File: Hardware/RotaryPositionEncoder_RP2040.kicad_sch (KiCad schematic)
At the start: 66 parts, among them J1 Conn_ABI, J2 Conn_UVW, J3 Conn_SWD, J4 USB_C_Receptacle_USB2.0, J5 Conn_5VDC, J6 Conn_CAN, U1 AS5047P, U2 RP2040, U3 M24C02-RMN, U3 RT9013-33GB, U4 W25Q32JVSS, U5 TJA1042T, Y1 Crystal_GND24

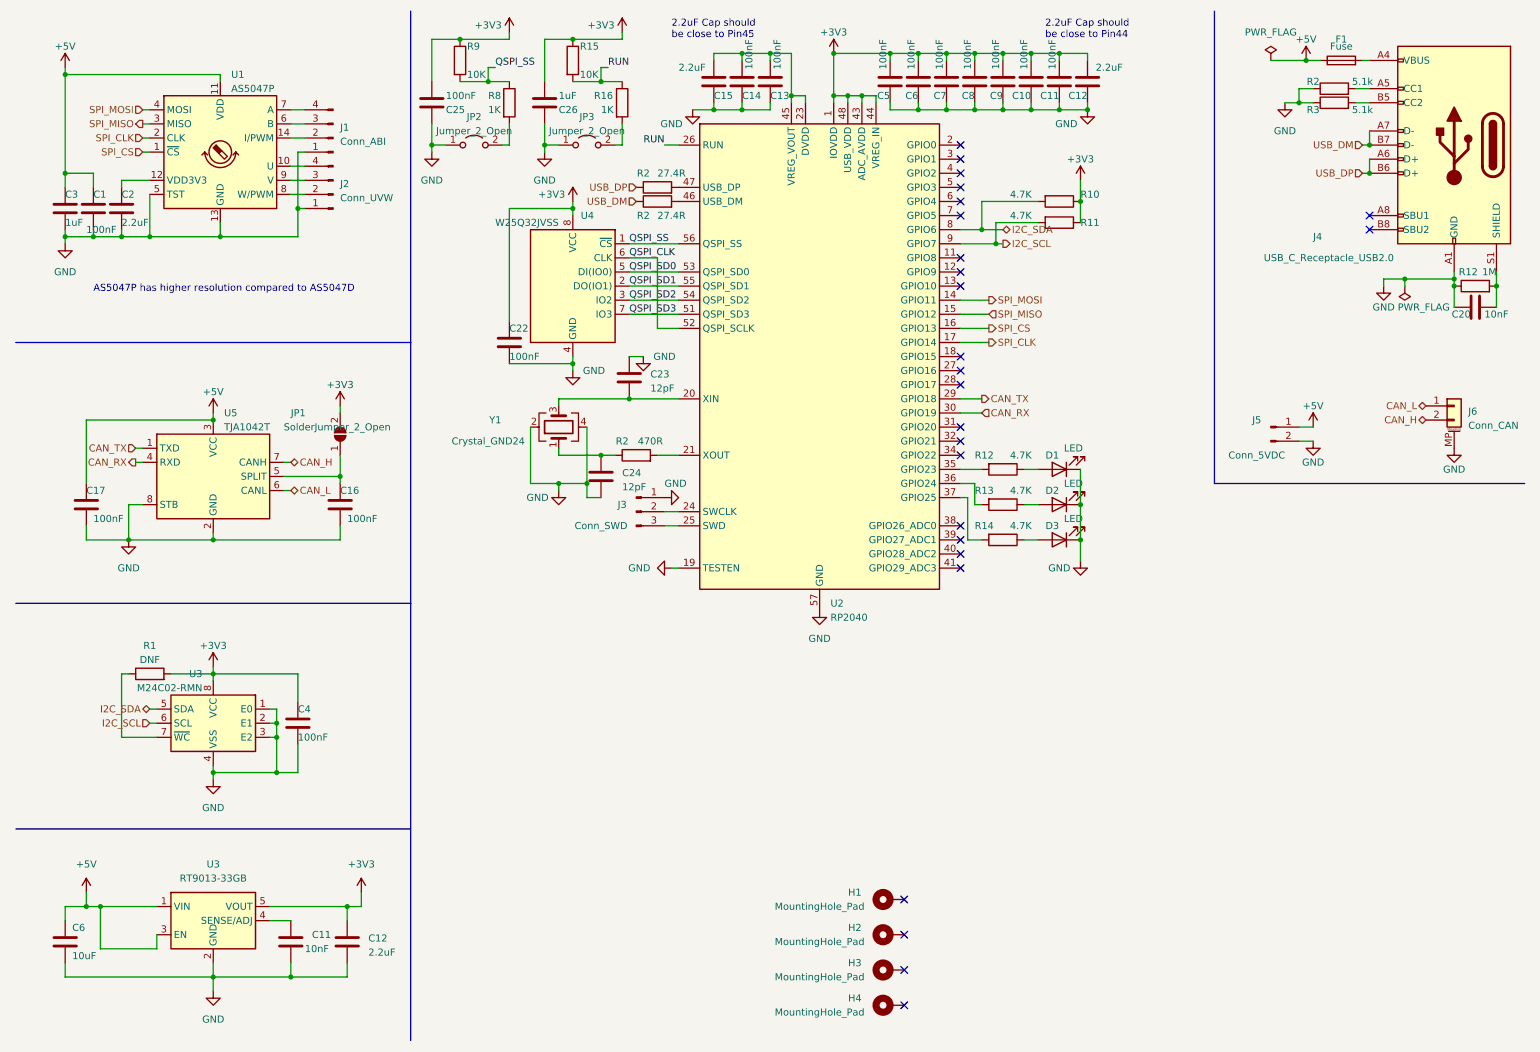
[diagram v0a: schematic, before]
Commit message: sch modify pcb init
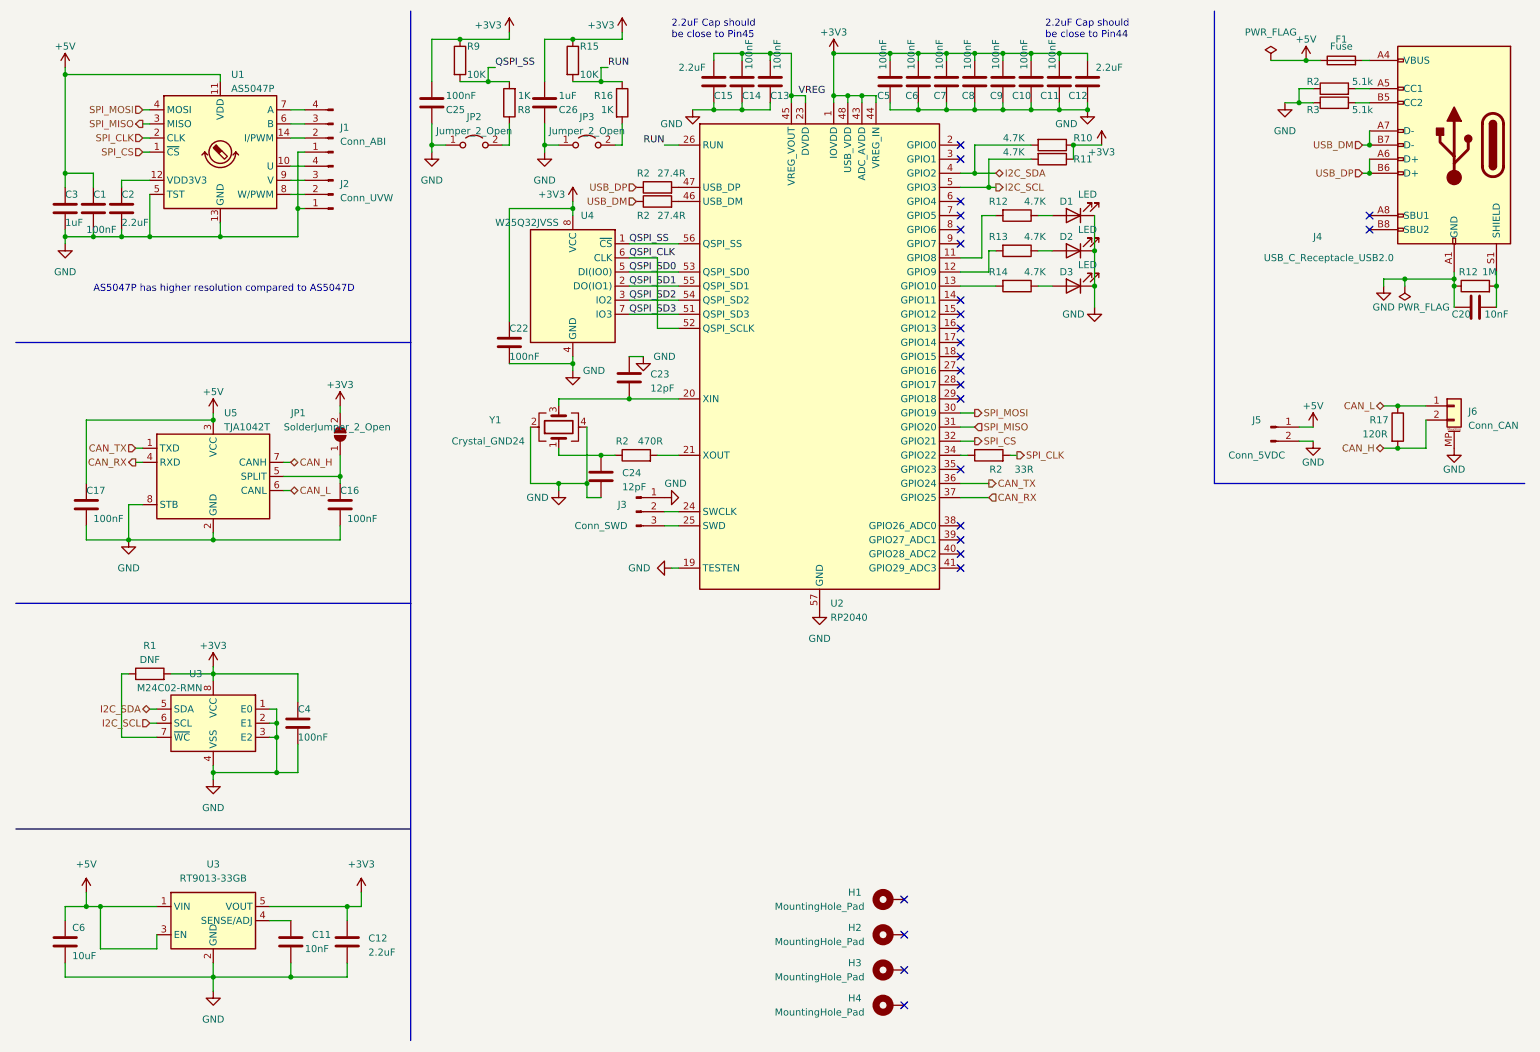
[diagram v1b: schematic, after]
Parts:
- added R17: 120R, Resistor_SMD:R_0603_1608Metric, symbol Device:R
- added R2: 33R, Resistor_SMD:R_0603_1608Metric, symbol Device:R
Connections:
- net CAN_H: now also R17.2
- net CAN_L: now also R17.1
- net CAN_RX: now also U2.37 (GPIO25); no longer U2.30 (GPIO19)
- net CAN_TX: now also U2.36 (GPIO24); no longer U2.29 (GPIO18)
- net I2C_SCL: now also U2.5 (GPIO3); no longer U2.9 (GPIO7)
- net I2C_SDA: now also U2.4 (GPIO2); no longer U2.8 (GPIO6)
- net QSPI_SS: now also R8.2; no longer R8.1
- net SPI_CLK: now also R2.2; no longer U2.17 (GPIO14)
- net SPI_CS: now also U2.32 (GPIO21); no longer U2.16 (GPIO13)
- net SPI_MISO: now also U2.31 (GPIO20); no longer U2.15 (GPIO12)
- net SPI_MOSI: now also U2.30 (GPIO19); no longer U2.14 (GPIO11)
- net at JP2.2 (B): now also R8.1; no longer R8.2
- net at R13.2: now also U2.12 (GPIO9); no longer U2.36 (GPIO24)
- net at U2.11 (GPIO8): now also R12.2
- net at U2.13 (GPIO10): now also R14.2
- net VREG: now reaches C13.2, C14.2, C15.2, U2.23 (DVDD), U2.45 (VREG_VOUT), U2.50 (DVDD)
- net at U2.34 (GPIO22): now also R2.1
- net at U2.35 (GPIO23): no longer R12.2
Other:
- moved on the sheet: R8

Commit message: add rs485
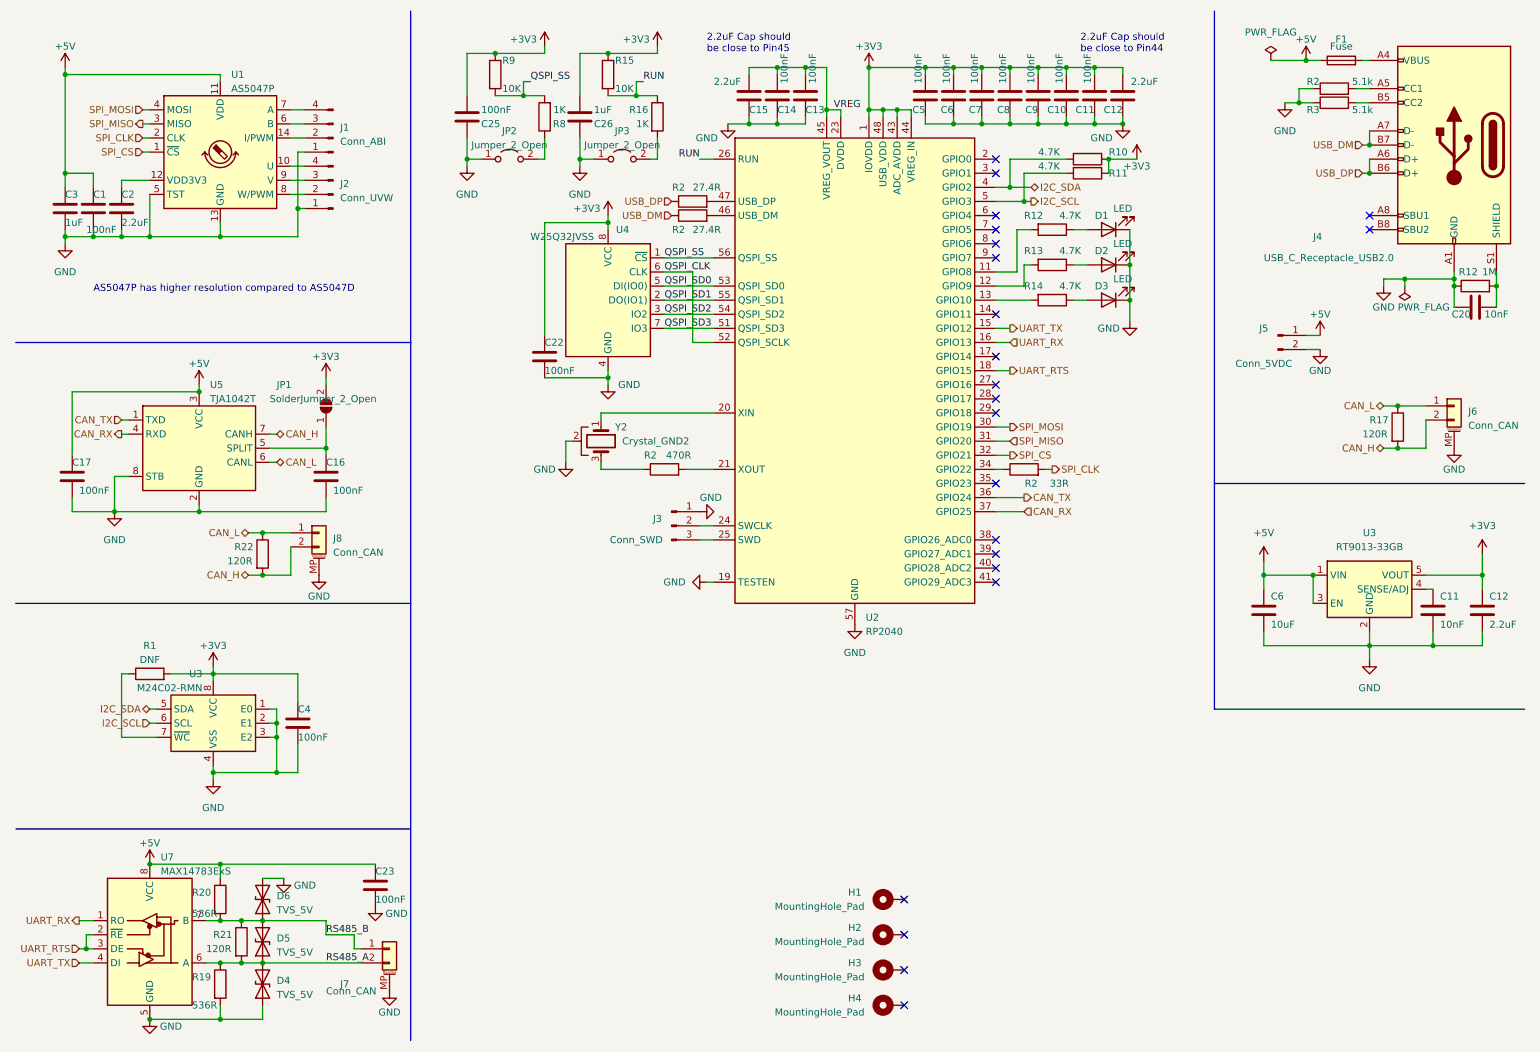
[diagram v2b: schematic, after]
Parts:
- removed C24: 12pF, Capacitor_SMD:C_0603_1608Metric, symbol Device:C
- removed Y1: Crystal_GND24, Crystal:Crystal_SMD_3225-4Pin_3.2x2.5mm_HandSoldering, symbol Device:Crystal_GND24
- added D4, D5, D6: TVS_5V, Diode_SMD:D_SMA_Handsoldering, symbol Device:D_TVS
- added J7, J8: Conn_CAN, Connector_JST:JST_GH_BM02B-GHS-TBT_1x02-1MP_P1.25mm_Vertical, symbol Connector_Generic_MountingPin:Conn_01x02_MountingPin
- added R19, R20: 536R, Resistor_SMD:R_0603_1608Metric, symbol Device:R
- added R21, R22: 120R, Resistor_SMD:R_0603_1608Metric, symbol Device:R
- added U7: MAX14783ExS, Package_SO:SOIC-8_3.9x4.9mm_P1.27mm, symbol Interface_UART:MAX14783ExS
- added Y2: Crystal_GND2, Crystal:Resonator_SMD_Murata_CSTxExxV-3Pin_3.0x1.1mm_HandSoldering, symbol Device:Crystal_GND2
- C23: value 12pF -> 100nF
- J1, J2: footprint Connector_PinHeader_2.54mm:PinHeader_1x04_P2.54mm_Horizontal -> Connector_JST:JST_GH_BM04B-GHS-TBT_1x04-1MP_P1.25mm_Vertical
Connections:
- net +5V: now also C23.1, R20.1, U7.8 (VCC)
- net CAN_H: now also J8.2 (Pin_2), R22.2
- net CAN_L: now also J8.1 (Pin_1), R22.1
- net GND: now also C23.2, D4.1 (A1), D6.2 (A2), J7.MP (MountPin), J8.MP (MountPin), R19.2, U7.5 (GND), Y2.2; no longer C23.1
- net at U2.20 (XIN): now also Y2.1; no longer C23.2
- net UART_TX: now reaches U2.15 (GPIO12)
- net UART_TX: now also U7.4 (DI)
- net UART_RX: now reaches U2.16 (GPIO13)
- net UART_RX: now also U7.1 (RO)
- net UART_RTS: now reaches U2.18 (GPIO15)
- net UART_RTS: now also U7.2 (~{RE}), U7.3 (DE)
- net at R2.1: now also Y2.3
- new net RS485_A: D4.2 (A2), D5.1 (A1), J7.2 (Pin_2), R19.1, R21.2, U7.6 (A)
- new net RS485_B: D5.2 (A2), D6.1 (A1), J7.1 (Pin_1), R20.2, R21.1, U7.7 (B)
- no-connect marks 25 -> 22
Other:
- moved on the sheet: C10, C11, C12, C13, C14, C15, C16, C17, C22, C25, C26, C5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

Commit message: fix: CAN/RS485 connector footprint change: TVS -> NUP2105 change: Flash SOP->WSOP
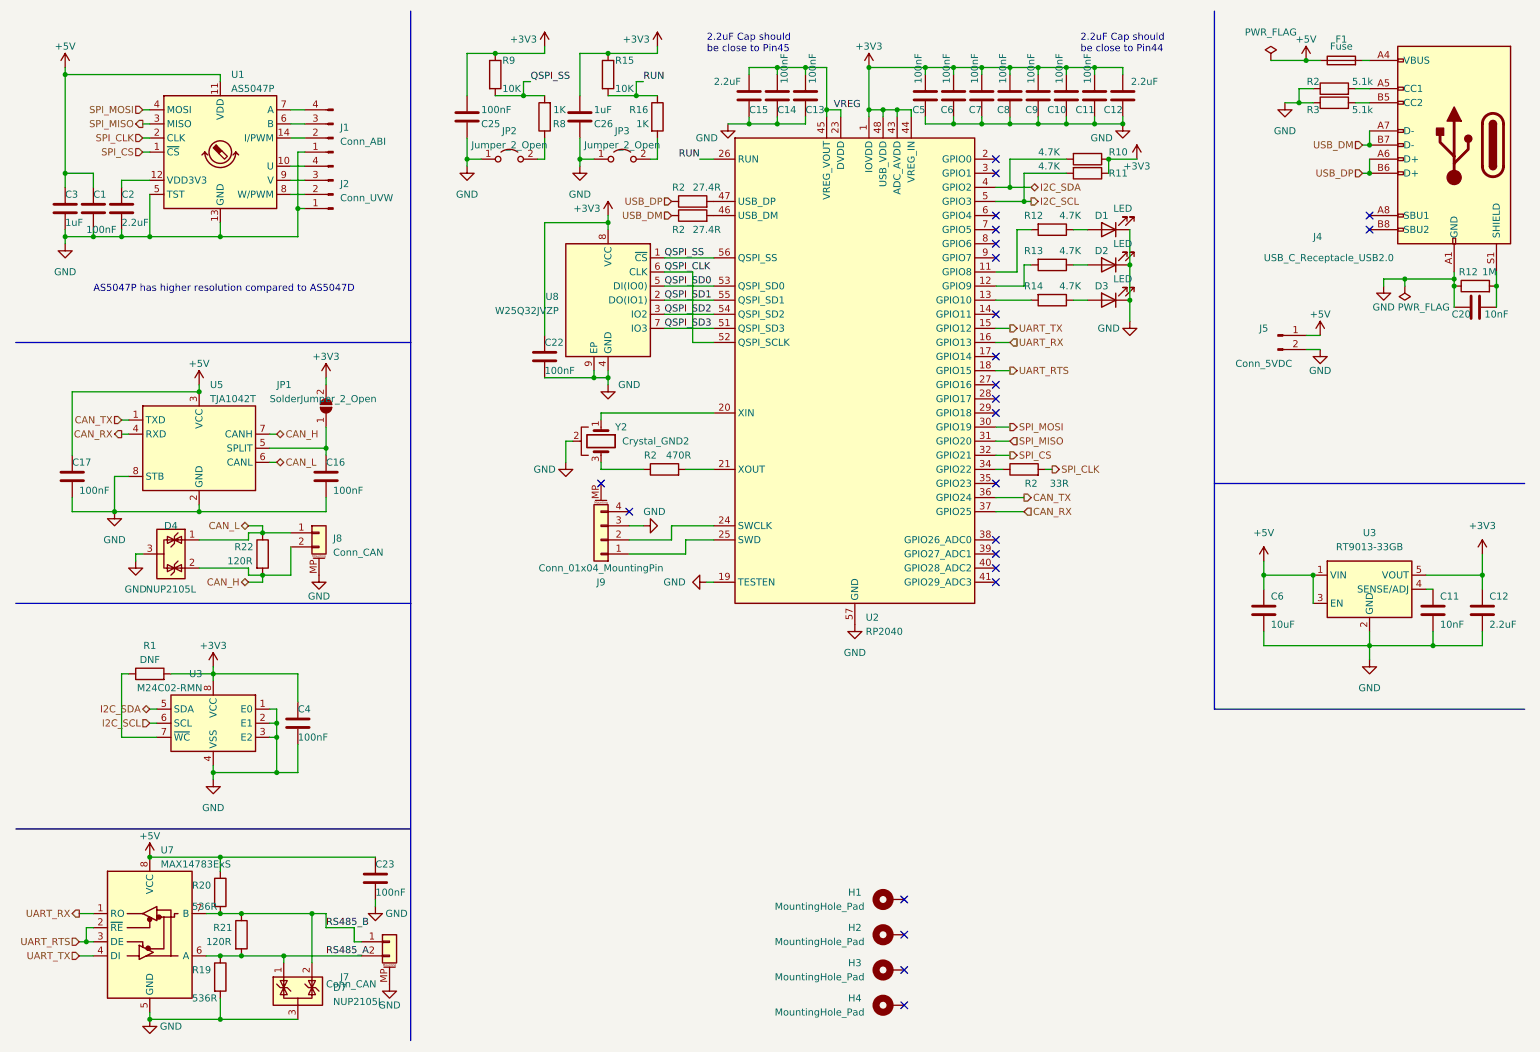
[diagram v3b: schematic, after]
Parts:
- removed D4, D5, D6: TVS_5V, Diode_SMD:D_SMA_Handsoldering, symbol Device:D_TVS
- removed J3: Conn_SWD, Connector_PinHeader_2.54mm:PinHeader_1x03_P2.54mm_Vertical, symbol Connector:Conn_01x03_Pin
- removed J6: Conn_CAN, Connector_JST:JST_GH_BM02B-GHS-TBT_1x02-1MP_P1.25mm_Vertical, symbol Connector_Generic_MountingPin:Conn_01x02_MountingPin
- removed R17: 120R, Resistor_SMD:R_0603_1608Metric, symbol Device:R
- removed U4: W25Q32JVSS, Package_SO:SOIC-8_5.23x5.23mm_P1.27mm, symbol Memory_Flash:W25Q32JVSS
- added D4, D7: NUP2105L, Package_TO_SOT_SMD:SOT-23, symbol Power_Protection:NUP2105L
- added J9: Conn_01x04_MountingPin, Connector_Molex:Molex_PicoBlade_53261-0471_1x04-1MP_P1.25mm_Horizontal, symbol Connector_Generic_MountingPin:Conn_01x04_MountingPin
- added U8: W25Q32JVZP, Package_SON:WSON-8-1EP_6x5mm_P1.27mm_EP3.4x4.3mm, symbol Memory_Flash:W25Q32JVZP
- J7, J8: footprint Connector_JST:JST_GH_BM02B-GHS-TBT_1x02-1MP_P1.25mm_Vertical -> Connector_JST:JST_GH_SM02B-GHS-TB_1x02-1MP_P1.25mm_Horizontal
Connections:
- net +3V3: now also U8.8 (VCC)
- net CAN_H: now also D4.2 (K)
- net CAN_L: now also D4.1 (K)
- net GND: now also D4.3 (A), D7.3 (A), J9.3 (Pin_3), U8.4 (GND), U8.9 (EP)
- net QSPI_CLK: now also U8.6 (CLK)
- net QSPI_SD0: now also U8.5 (DI(IO0))
- net QSPI_SD1: now also U8.2 (DO(IO1))
- net QSPI_SD2: now also U8.3 (IO2)
- net QSPI_SD3: now also U8.7 (IO3)
- net QSPI_SS: now also U8.1 (~{CS})
- net RS485_A: now also D7.1 (K)
- net RS485_B: now also D7.2 (K)
- net at U2.24 (SWCLK): now also J9.2 (Pin_2)
- net at U2.25 (SWD): now also J9.1 (Pin_1)
- no-connect marks 22 -> 24
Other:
- moved on the sheet: C23, J7, R19, R20, R21, U7
